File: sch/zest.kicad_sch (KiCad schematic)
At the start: 1 part, among them J4 ERF8-025-05.0-L-DV-L-K-TR

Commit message: added tps and new init layout
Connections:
- net GND: now also J4.03, J4.05, J4.16, J4.18, J4.24, J4.26, J4.27, J4.29, J4.32, J4.34, J4.35, J4.37, J4.40, J4.42, J4.43, J4.45
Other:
- moved on the sheet: J4

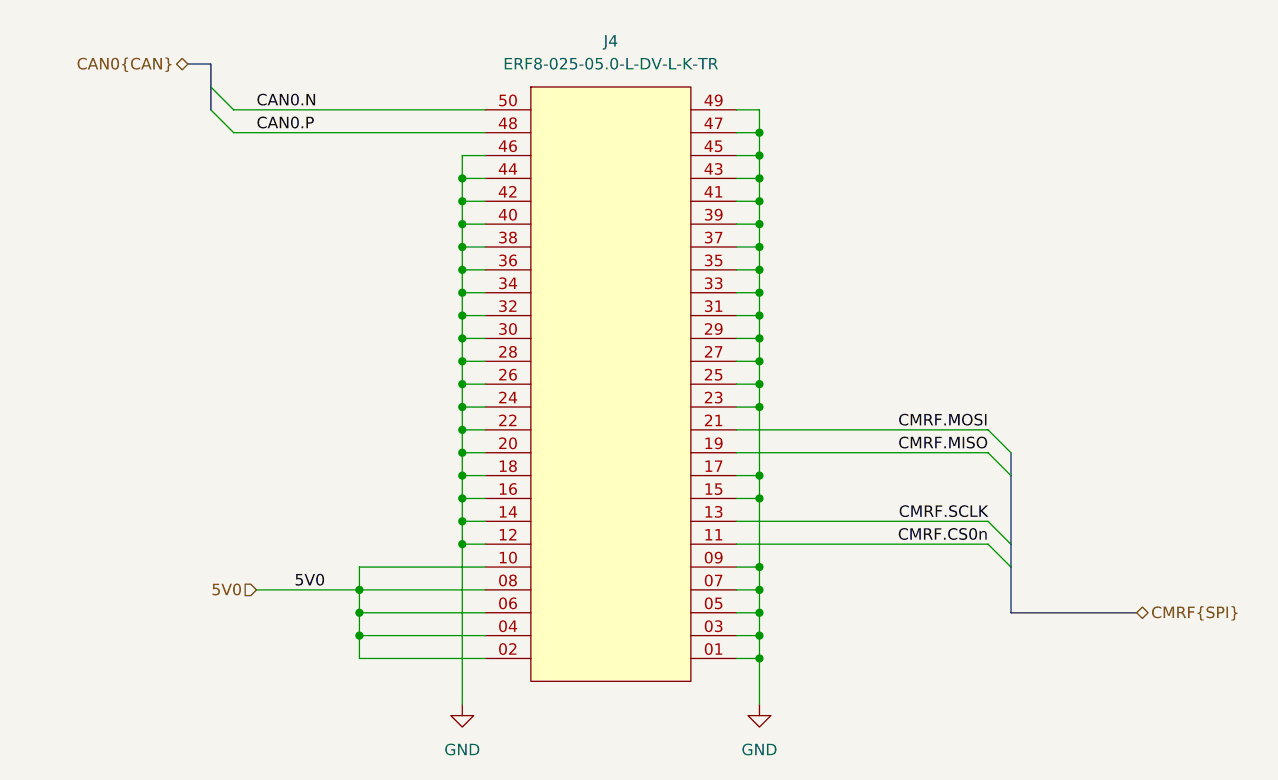
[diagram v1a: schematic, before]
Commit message: rev b, flipped connectors
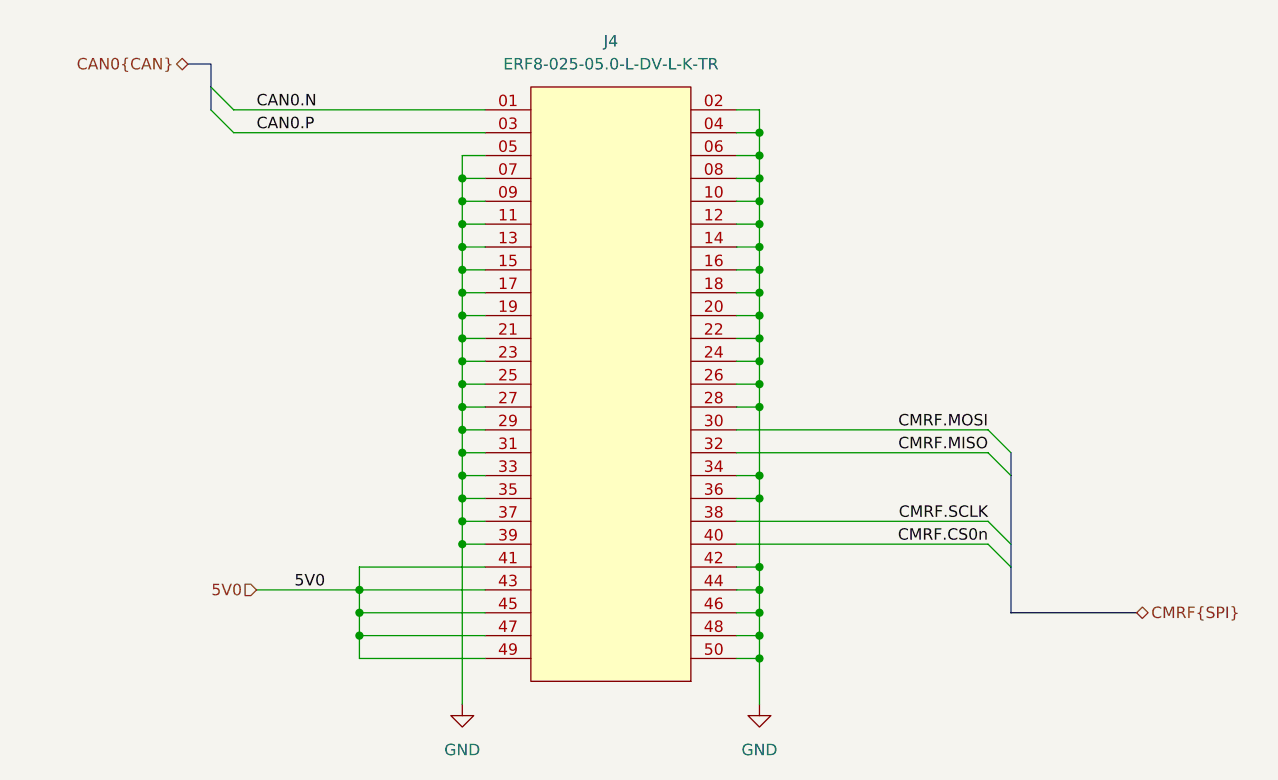
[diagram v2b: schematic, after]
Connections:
- net 5V0: now also J4.41, J4.43, J4.45, J4.47, J4.49; no longer J4.02, J4.04, J4.06, J4.08, J4.10
- net CAN0.N: now also J4.01; no longer J4.50
- net CAN0.P: now also J4.03; no longer J4.48
- net CMRF.CS0n: now also J4.40; no longer J4.11
- net CMRF.MISO: now also J4.32; no longer J4.19
- net CMRF.MOSI: now also J4.30; no longer J4.21
- net CMRF.SCLK: now also J4.38; no longer J4.13
- net GND: now also J4.02, J4.04, J4.06, J4.08, J4.10, J4.11, J4.13, J4.19, J4.21, J4.48, J4.50; no longer J4.01, J4.03, J4.30, J4.32, J4.38, J4.40, J4.41, J4.43, J4.45, J4.47, J4.49
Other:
- moved on the sheet: J4
